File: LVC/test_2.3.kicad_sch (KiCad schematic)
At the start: 5 parts, among them U1 TL431DBZ

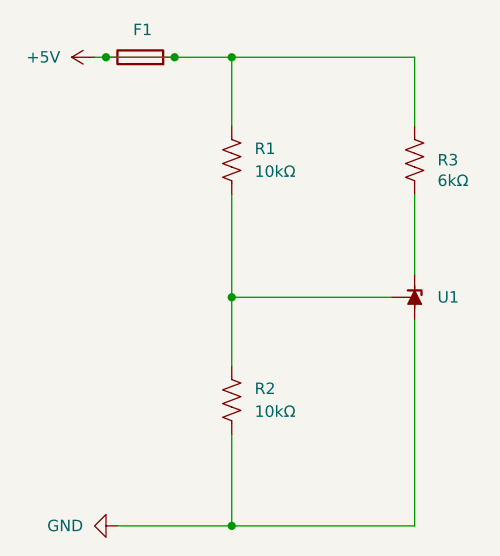
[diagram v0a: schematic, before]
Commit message: Refining Schematics
Refined the visuals of all the schematics to remove values from components. Also removed a redundant schematic.
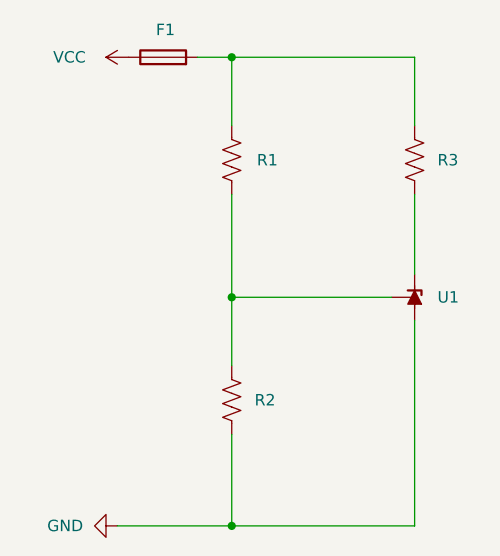
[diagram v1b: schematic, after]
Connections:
- net +5V: no longer F1.2, R1.1, R3.1
- new net: F1.2, R1.1, R3.1
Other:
- moved on the sheet: F1
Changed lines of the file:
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@@
-	)
-	(junction
-		(at 86.36 54.61)
-		(diameter 0)
-		(color 0 0 0 0)
-	)
-	(junction
-		(at 93.98 54.61)
-		(diameter 0)
-		(color 0 0 0 0)
 	)
 	(junction
@@
 	(wire
 		(pts
-			(xy 86.36 54.61) (xy 93.98 54.61)
-		)
-		(stroke
-			(width 0)
-			(type default)
-		)
-	)
-	(wire
-		(pts
 			(xy 100.33 81.28) (xy 100.33 88.9)
 		)
@@
 	(wire
 		(pts
-			(xy 93.98 54.61) (xy 100.33 54.61)
-		)
-		(stroke
-			(width 0)
-			(type default)
-		)
-	)
-	(wire
-		(pts
 			(xy 100.33 96.52) (xy 100.33 106.68)
 		)
@@
 	(wire
 		(pts
+			(xy 96.52 54.61) (xy 100.33 54.61)
+		)
+		(stroke
+			(width 0)
+			(type default)
+		)
+	)
+	(wire
+		(pts
 			(xy 100.33 54.61) (xy 120.65 54.61)
 		)
@@
 		(pts
 			(xy 87.63 106.68) (xy 100.33 106.68)
-		)
-		(stroke
-			(width 0)
-			(type default)
-		)
-	)
-	(wire
-		(pts
-			(xy 85.09 54.61) (xy 86.36 54.61)
 		)
 		(stroke
@@
 		(property "Value" "6kΩ"
 			(at 123.19 68.326 0)
+			(hide yes)
 			(show_name no)
 			(do_not_autoplace no)
@@
 		(in_pos_files yes)
 		(dnp no)
-		(fields_autoplaced yes)
 		(property "Reference" "R2"
-			(at 102.87 91.4399 0)
+			(at 102.87 92.71 0)
 			(show_name no)
 			(do_not_autoplace no)
@@
 		(property "Value" "10kΩ"
 			(at 102.87 93.9799 0)
+			(hide yes)
 			(show_name no)
 			(do_not_autoplace no)
@@
 	(symbol
 		(lib_id "power:VCC")
-		(at 85.09 54.61 90)
+		(at 88.9 54.61 90)
 		(unit 1)
 		(body_style 1)
@@
 		(in_pos_files yes)
 		(dnp no)
-		(fields_autoplaced yes)
-		(property "Reference" "#PWR09"
+		(property "Reference" "VCC"
+			(at 82.296 54.61 90)
+			(show_name no)
+			(do_not_autoplace no)
+			(effects
+				(font
+					(size 1.27 1.27)
+				)
+			)
+		)
+		(property "Value" "+5V"
+			(at 85.09 54.6099 90)
+			(hide yes)
+			(show_name no)
+			(do_not_autoplace no)
+			(effects
+				(font
+					(size 1.27 1.27)
+				)
+				(justify left)
+			)
+		)
+		(property "Footprint" ""
 			(at 88.9 54.61 0)
 			(hide yes)
@@
 			)
 		)
-		(property "Value" "+5V"
-			(at 81.28 54.6099 90)
-			(show_name no)
-			(do_not_autoplace no)
-			(effects
-				(font
-					(size 1.27 1.27)
-				)
-				(justify left)
-			)
-		)
-		(property "Footprint" ""
-			(at 85.09 54.61 0)
-			(hide yes)
-			(show_name no)
-			(do_not_autoplace no)
-			(effects
-				(font
-					(size 1.27 1.27)
-				)
-			)
-		)
 		(property "Datasheet" ""
-			(at 85.09 54.61 0)
+			(at 88.9 54.61 0)
 			(hide yes)
 			(show_name no)
@@
 		)
 		(property "Description" "Power symbol creates a global label with name \"VCC\""
-			(at 85.09 54.61 0)
+			(at 88.9 54.61 0)
 			(hide yes)
 			(show_name no)
@@
 			(project "LVC"
 				(path "/424f3e55-bd99-4bdd-822e-1fe4d61e0272"
-					(reference "#PWR09")
+					(reference "VCC")
 					(unit 1)
 				)
@@
 	(symbol
 		(lib_id "Device:Fuse")
-		(at 90.17 54.61 90)
+		(at 92.71 54.61 90)
 		(unit 1)
 		(body_style 1)
@@
 		(dnp no)
 		(property "Reference" "F1"
-			(at 90.424 51.562 90)
+			(at 92.964 51.562 90)
 			(show_name no)
 			(do_not_autoplace no)
@@
 		)
 		(property "Value" "Fuse"
-			(at 90.17 50.8 90)
+			(at 92.71 50.8 90)
 			(hide yes)
 			(show_name no)
@@
 		)
 		(property "Footprint" ""
-			(at 90.17 56.388 90)
+			(at 92.71 56.388 90)
 			(hide yes)
 			(show_name no)
@@
 		)
 		(property "Datasheet" ""
-			(at 90.17 54.61 0)
+			(at 92.71 54.61 0)
 			(hide yes)
 			(show_name no)
@@
 		)
 		(property "Description" "Fuse"
-			(at 90.17 54.61 0)
+			(at 92.71 54.61 0)
 			(hide yes)
 			(show_name no)
@@
 		(in_pos_files yes)
 		(dnp no)
-		(fields_autoplaced yes)
 		(property "Reference" "R1"
-			(at 102.87 64.7699 0)
+			(at 103.124 66.04 0)
 			(show_name no)
 			(do_not_autoplace no)
@@
 		(property "Value" "10kΩ"
 			(at 102.87 67.3099 0)
-			(show_name no)
-			(do_not_autoplace no)
+			(hide yes)
+			(show_name no)
+			(do_not_autoplace no)
